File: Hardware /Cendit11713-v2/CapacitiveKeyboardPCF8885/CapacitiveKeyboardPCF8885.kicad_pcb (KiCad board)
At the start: 2 copper layers, 49 parts, among them P1 I2C_CONN_01X08, P10 PLATE_CONN, P2 DEBUG_CONN_01X11, P3 PLATE_CONN, P4 PLATE_CONN, P5 PLATE_CONN, P6 PLATE_CONN, P7 PLATE_CONN, P8 PLATE_CONN, P9 PLATE_CONN, U1 PCF8885

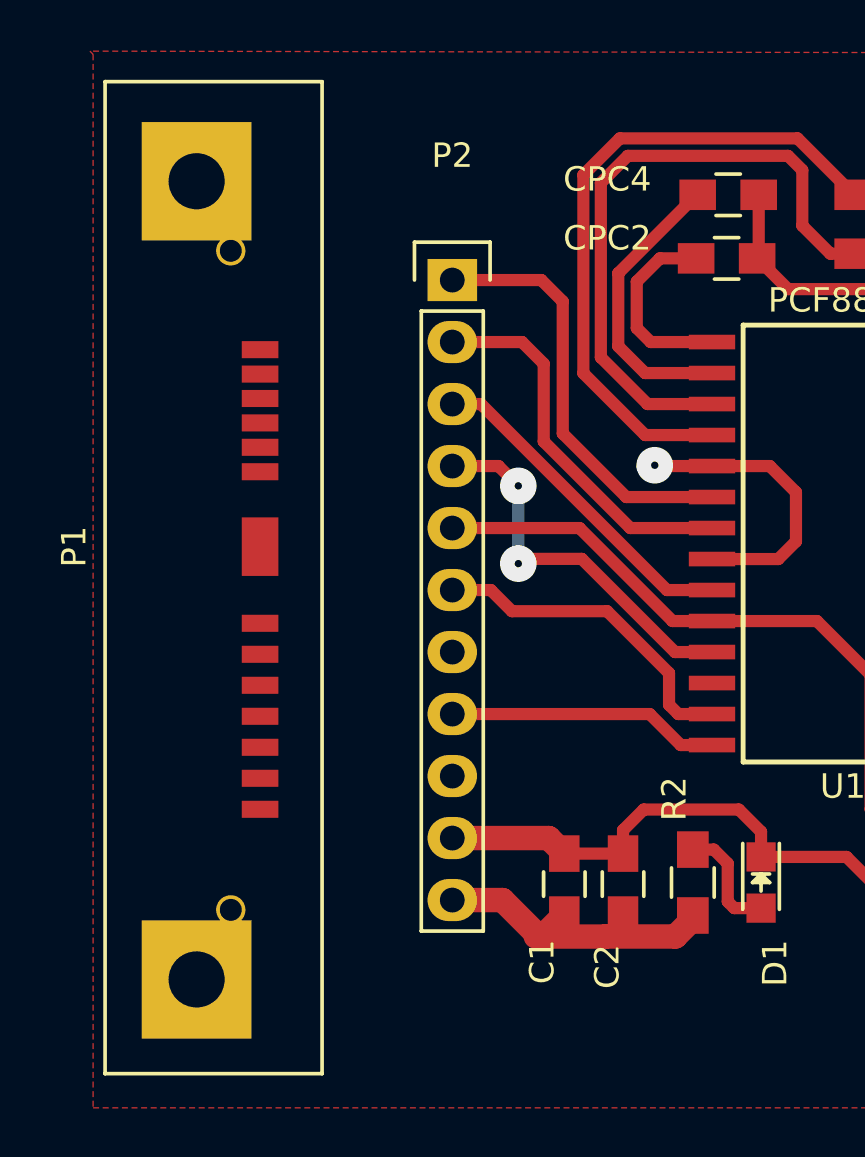
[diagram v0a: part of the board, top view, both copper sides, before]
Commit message: Trabajo en CenditLab.Reducido + Cendit11713 PCB
   - CenditLab clases para manejo de setup ENR
   - Clase field para dato temperatura
   - Edición de PCBs Capacitive Keyboard
   - Edición de esquematico MainBoard con PIC18F4550 DIP
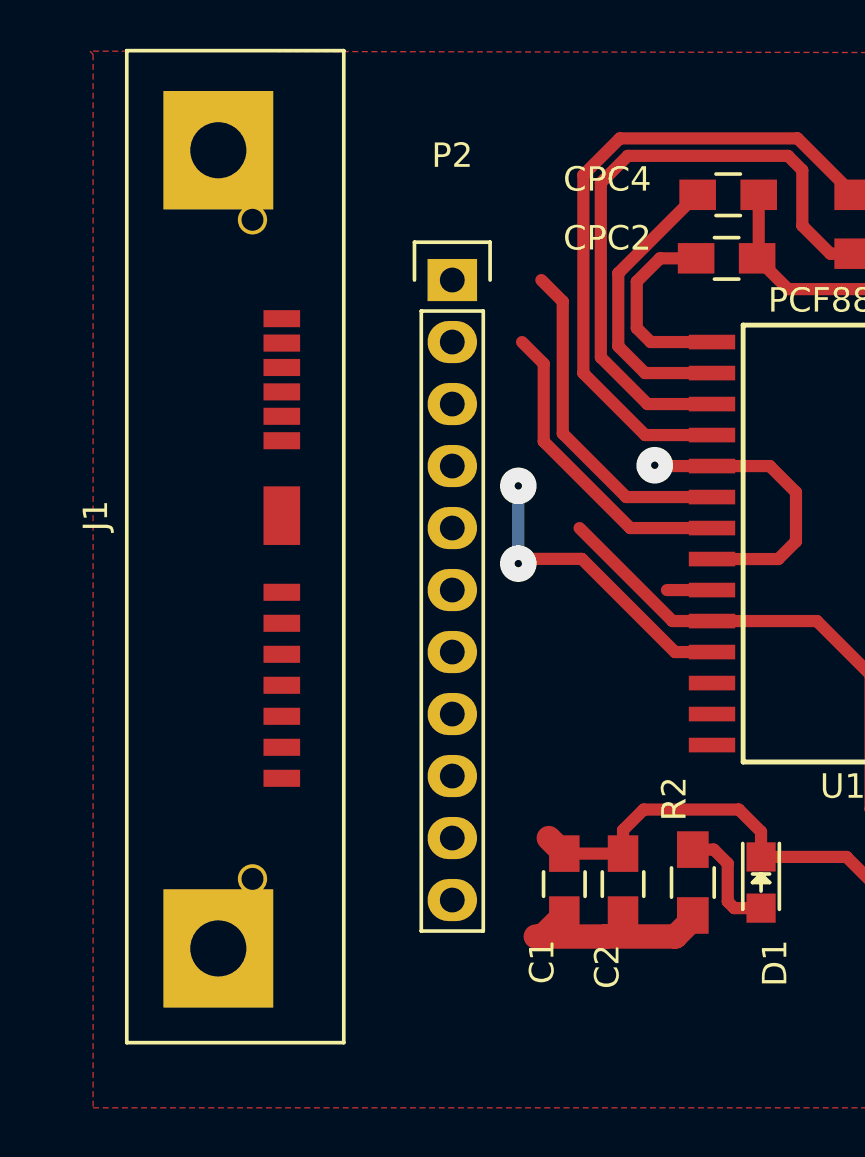
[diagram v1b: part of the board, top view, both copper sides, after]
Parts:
- removed P1: I2C_CONN_01X08, CenditFootprints:SLIMLINE_SATA_PLUG_7P_6P
- added J1: I2C_CONN_01X13, CenditFootprints:SLIMLINE_SATA_PLUG_7P_6P, F.Cu at (104.8, 83.2)
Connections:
- P2 pad 1: /SCL -> +3V3
- P2 pad 10: GNDA -> /CLK_IN
- P2 pad 11: +3V3 -> /CLK_OUT
- P2 pad 2: /SDA -> GNDA
- P2 pad 3: /A0 -> VDD
- P2 pad 4: //INT -> /SDA
- P2 pad 5: /SLEEP -> /SCL
- P2 pad 6: //INT_IN -> /A0
- P2 pad 7: /CLK_OUT -> //INT
- P2 pad 8: /CLK_IN -> /SLEEP
- P2 pad 9: VDD -> //INT_IN
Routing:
- net //INT_IN: track 13.5 -> 0.00 mm
- net /A0: track 13.8 -> 1.85 mm
- net /CLK_IN: track 11.2 -> 0.00 mm
- net /SLEEP: track 27.6 -> 22.4 mm
- net +3V3: track 13.7 -> 9.48 mm
- net GNDA: track 408.1 -> 404.2 mm
- net /SCL: track 17.5 -> 13.8 mm
- net //INT: track 15.8 -> 12.8 mm
- net /SDA: track 15.7 -> 12.8 mm

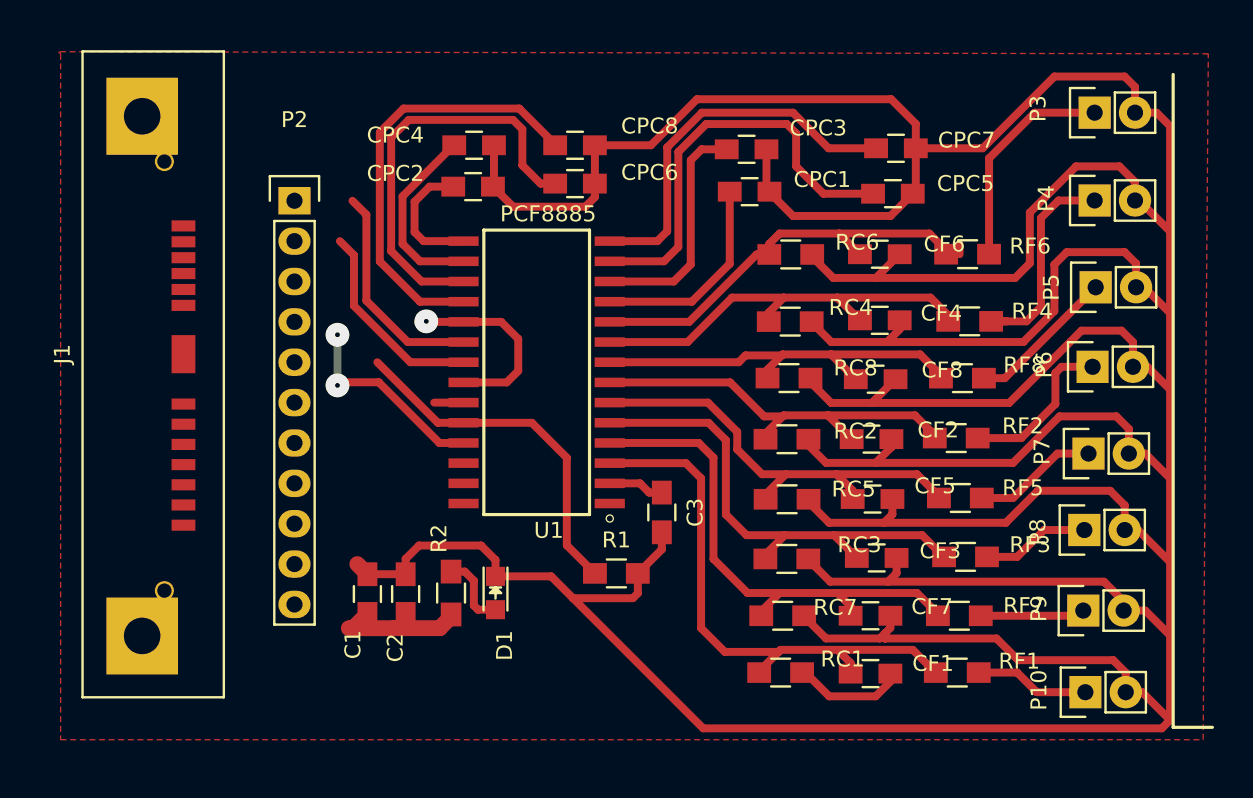
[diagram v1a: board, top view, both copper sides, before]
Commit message: Trabajo en Cendit11713
  - Revision de esquematicos + PCBs
  - Generacion de archivos Gerber
  - CapacitiveKeyboard -> edicion PCB
  - Inicia PCB GpibPortExpander
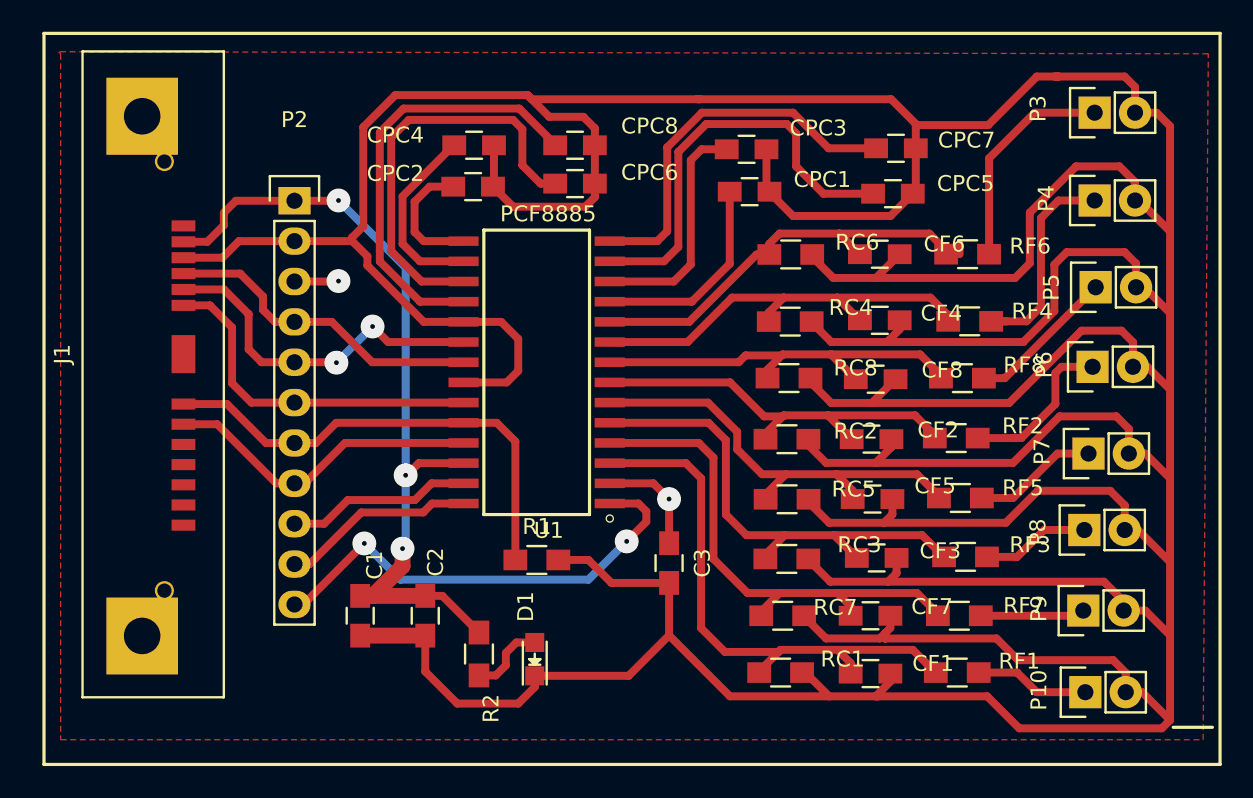
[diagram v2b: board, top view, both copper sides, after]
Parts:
- moved R1 5.08 mm to (127.0, 96.1)
- moved D1 4.84 mm to (126.9, 102.4), turned to 90 degrees
- moved R2 4.22 mm to (123.4, 102.0), turned to 270 degrees
- moved C3 3.22 mm to (135.3, 96.3)
- moved C2 1.84 mm to (120.0, 99.6), turned to 270 degrees
- moved C1 1.44 mm to (115.9, 99.6), turned to 270 degrees
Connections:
- J1 pad 7: //INT -> /SLEEP
- J1 pad 8: /SLEEP -> //INT
- P2 pad 7: //INT -> /SLEEP
- P2 pad 8: /SLEEP -> //INT
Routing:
- net GNDA: track 404.2 -> 449.6 mm, vias 1 -> 0
- net +3V3: track 9.48 -> 51.8 mm, vias 0 -> 3
- net /CLK_OUT: track 0.00 -> 29.4 mm, vias 0 -> 2
- net /A0: track 1.85 -> 22.2 mm
- net //INT_IN: track 0.00 -> 12.3 mm
- net /CLK_IN: track 0.00 -> 12.2 mm
- net /SCL: track 13.8 -> 22.3 mm, vias 0 -> 2
- net /SLEEP: track 22.4 -> 30.4 mm
- net /SDA: track 12.8 -> 20.4 mm
- net //INT: track 12.8 -> 20.2 mm, vias 2 -> 0
- net VDD: track 3.52 -> 10.0 mm, vias 0 -> 2

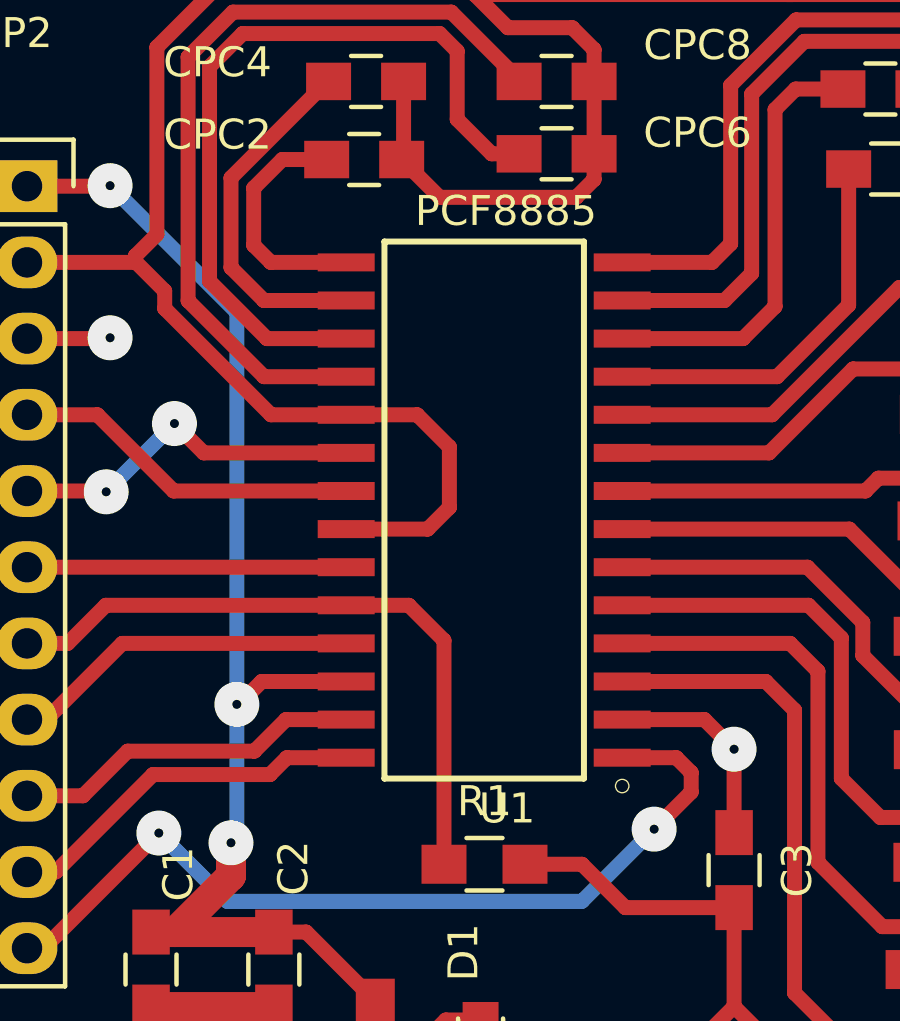
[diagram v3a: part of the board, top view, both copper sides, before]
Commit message: En Cendit11713 edicion de esquematicos + revision PCBs
  - Edicion de esquematicos tarjeta madre
  - Revision de PCBs corrección de footprints
  - Descarga de footprints + creacion lib simbolos: RTC + sensor temp/hum
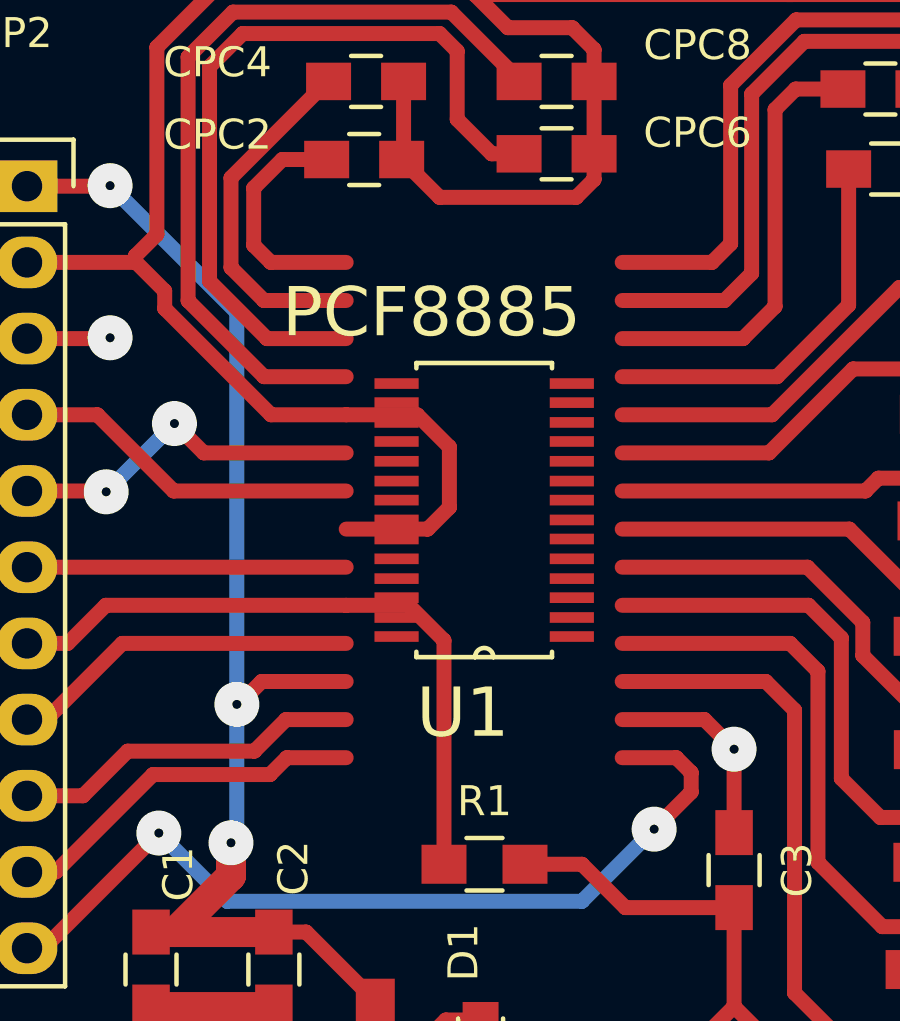
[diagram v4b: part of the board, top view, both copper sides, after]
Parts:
- U1: footprint LibKicad:PCF8885TS -> LibreriaKicad2:PCF8885TS
